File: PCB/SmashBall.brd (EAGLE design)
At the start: 27.5 x 27.5 mm, 7 parts

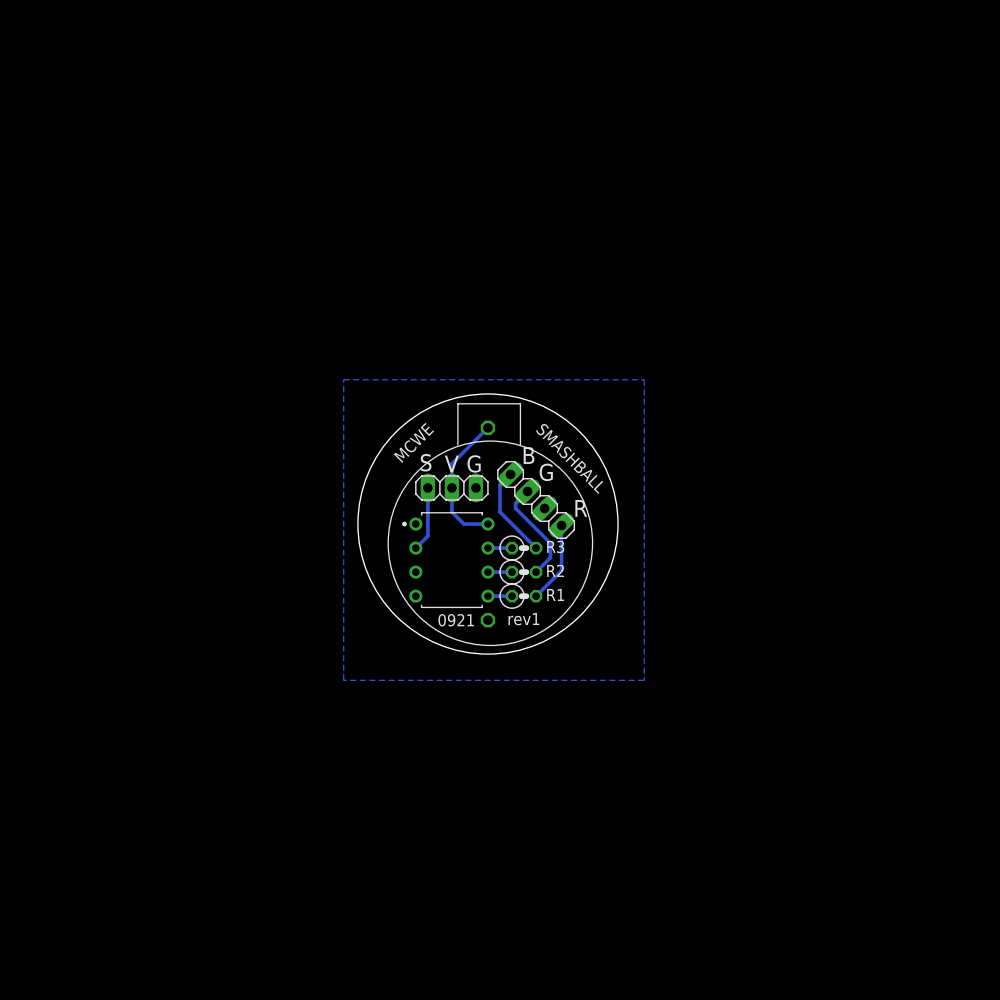
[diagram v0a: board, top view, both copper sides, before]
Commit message: Redid the schematic and am halfway through redoing the board design.
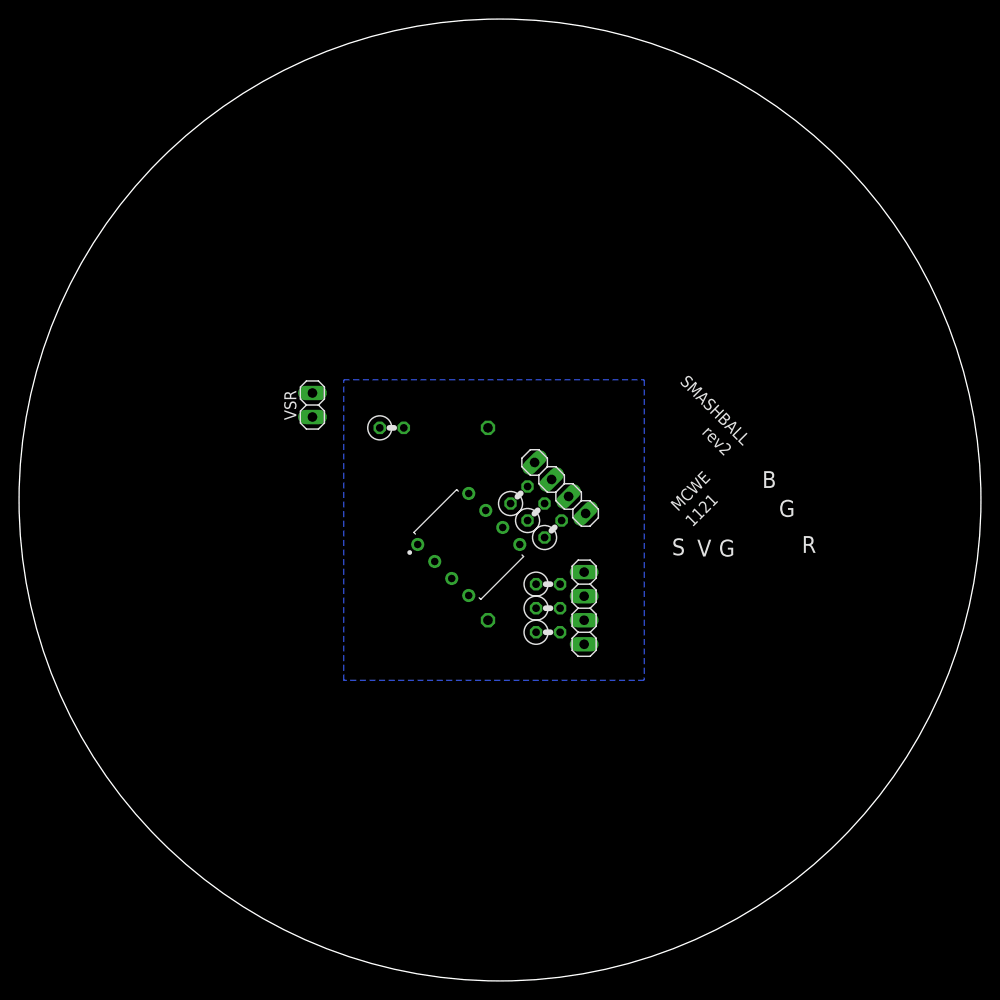
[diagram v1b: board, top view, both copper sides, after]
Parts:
- removed RATTLE_SWITCH: (no value), pinhead:1X03
- removed RGB_LED: (no value), pinhead:1X04
- added R4, R5, R6: (no value), rcl:0207/2V
- added R7: 10k, rcl:0207/2V
- added RGB_LED1, RGB_LED2: (no value), pinhead:1X04
- added VSR: (no value), pinhead:1X02
- moved R1 7.73 mm to (6.88, 2.01), turned to 45 degrees
- moved R2 6.48 mm to (5.08, 3.81), turned to 45 degrees
- moved R3 5.63 mm to (3.28, 5.61), turned to 45 degrees
- moved U$1 2.43 mm to (-2.03, 0.38), turned to 45 degrees
- flipped U$2 to the bottom
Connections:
- removed net N$1: R1.1, U$1.5
- removed net N$2: R2.1, U$1.6
- removed net N$3: R3.1, U$1.7
- new net BLUE1: R3.2, RGB_LED1.4
- new net BLUE2: R6.2, RGB_LED2.4
- new net GREEN1: R2.2, RGB_LED1.3
- new net GREEN2: R5.2, RGB_LED2.3
- new net RED1: R1.2, RGB_LED1.1
- new net RED2: R4.2, RGB_LED2.1
- net BLUE: now also R3.1, R6.1, U$1.7; no longer R3.2, RGB_LED.4
- net GND: now also RGB_LED1.2, RGB_LED2.2, VSR.2; no longer RATTLE_SWITCH.3, RGB_LED.2
- net GREEN: now also R2.1, R5.1, U$1.6; no longer R2.2, RGB_LED.3
- net RED: now also R1.1, R4.1, U$1.5; no longer R1.2, RGB_LED.1
- net SWTCH: now also R7.1, VSR.1; no longer RATTLE_SWITCH.1
- net VIN: now also R7.2; no longer RATTLE_SWITCH.2
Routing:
- net VIN: track 14.8 -> 0.00 mm
- net GREEN: track 11.2 -> 0.00 mm
- net BLUE: track 9.81 -> 0.00 mm
- net RED: track 8.58 -> 0.00 mm
- net SWTCH: track 6.88 -> 0.00 mm
- net N$3: track 2.54 -> 0.00 mm
- net N$2: track 2.54 -> 0.00 mm
- net N$1: track 2.54 -> 0.00 mm
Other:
- board size 27.5 x 27.5 mm -> 101.6 x 101.6 mm
- board text added: "1121"
- board text added: "rev2"
- board text removed: "0921"
- board text removed: "rev1"

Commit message: Finished layout of the board.
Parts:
- moved RGB_LED2 18.0 mm to (-7.77, -8.03), turned to 135 degrees
- moved VSR 16.0 mm to (-7.62, 3.43), turned to 270 degrees
- moved R6 14.3 mm to (-6.88, -3.54), turned to 225 degrees
- moved R5 11.5 mm to (-5.08, -5.33), turned to 225 degrees
- moved R4 10.2 mm to (-3.28, -7.13), turned to 225 degrees
- moved R7 8.85 mm to (-3.30, 7.11), turned to 90 degrees
- moved U$1 2.55 mm to (0.51, 0.13)
- moved R2 1.88 mm to (5.97, 5.46)
- moved R1 1.88 mm to (7.77, 3.66)
- moved R3 1.88 mm to (4.17, 7.26)
- moved RGB_LED1 1.88 mm to (8.51, 8.00)
- moved U$2 0.64 mm to (0.00, -8.26)
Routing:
- net RED: track 0.00 -> 15.8 mm
- net GREEN: track 0.00 -> 15.3 mm
- net BLUE: track 0.00 -> 15.3 mm
- net SWTCH: track 0.00 -> 12.4 mm
- net VIN: track 0.00 -> 11.8 mm
- net RED2: track 0.00 -> 3.07 mm
- net GREEN2: track 0.00 -> 3.07 mm
- net BLUE2: track 0.00 -> 3.07 mm
- net BLUE1: track 0.00 -> 2.85 mm
- net GREEN1: track 0.00 -> 2.85 mm
- net RED1: track 0.00 -> 2.39 mm
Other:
- board size 101.6 x 101.6 mm -> 29.2 x 29.2 mm
- board text added: "Love you Tommy!"
- board text removed: "B"
- board text removed: "G"
- board text removed: "R"
- board text removed: "S"
- board text removed: "V"
